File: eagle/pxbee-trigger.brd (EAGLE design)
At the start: 51 x 57 mm, 24 parts, among them J1 39501-1002, J2 39501-1009, K1 APAN3103, K2 APAN3103, K3 APAN3103, K4 APAN3103, Q1 BC548BTA, Q2 BC548BTA, Q3 BC548BTA, Q4 BC548BTA

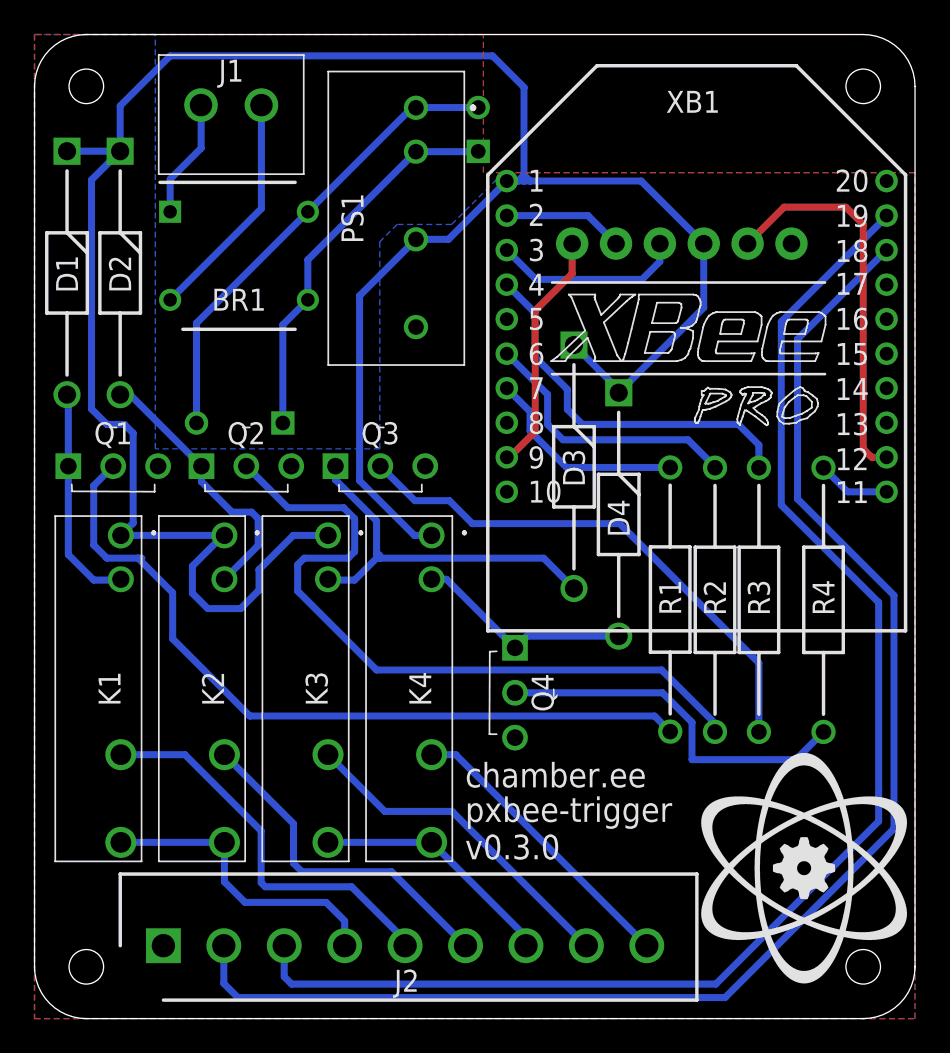
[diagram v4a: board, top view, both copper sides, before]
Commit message: Bridge rectifier upgrade; XBee reset header
- [Parts] Bridge rectifier upgraded from DF005 to DF01, previous part was underdimensioned
- [SCH,BRD] Added J3 pinout for XBee Reset
- [BRD] Version bumped to v0.4.0
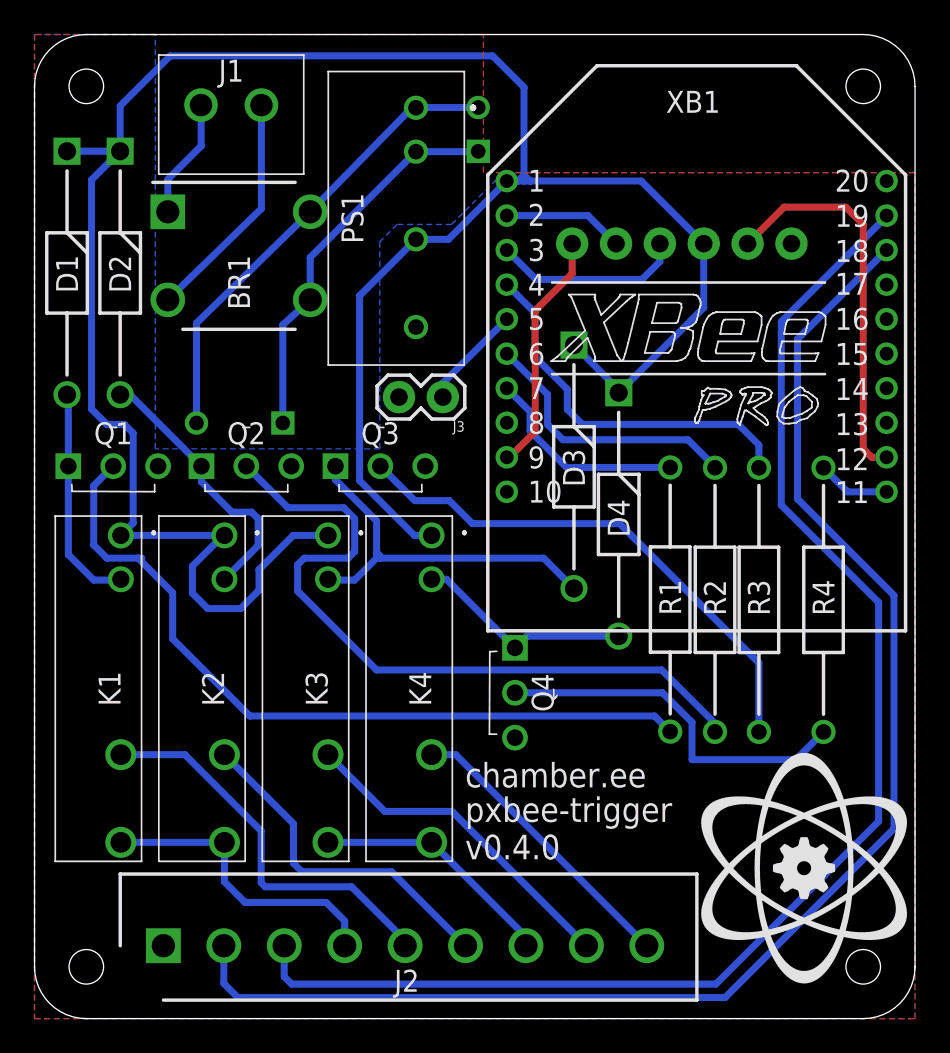
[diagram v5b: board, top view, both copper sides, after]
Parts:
- added J3: (no value), SparkFun-Connectors:1X02
- BR1: value DF005M -> DF01M; device parts:DIP798W58P510L828H330Q4N -> parts:DIP825W114P510L828H330Q4N
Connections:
- net DIO1 renamed STAT1
- net DIO2 renamed STAT2
- new net RST: J3.1, XB1.5
- net GND: now also J3.2
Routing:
- net RST: track 0.00 -> 6.05 mm
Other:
- board text added: "A1"
- board text added: "A2"
- board text added: "A3"
- board text added: "A4"
- board text added: "C1"
- board text added: "C2"
- board text added: "GND"
- board text added: "S1"
- board text added: "S2"
- board text added: "v0.4.0"
- board text removed: "v0.3.0"
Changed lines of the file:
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@@
 <text x="24.941" y="13.393" size="1.4224" layer="21" rot="R180" align="top-right">chamber.ee</text>
 <text x="24.941" y="11.393" size="1.4224" layer="21" rot="R180" align="top-right">pxbee-trigger</text>
-<text x="24.941" y="9.22755625" size="1.4224" layer="21" rot="R180" align="top-right">v0.3.0</text>
+<text x="24.941" y="9.22755625" size="1.4224" layer="21" rot="R180" align="top-right">v0.4.0</text>
 <hole x="3" y="3" drill="2"/>
 <hole x="48" y="3" drill="2"/>
@@
 <wire x1="3" y1="57" x2="0" y2="54" width="0" layer="20" curve="90"/>
 <wire x1="51" y1="54" x2="48" y2="57" width="0" layer="20" curve="90"/>
+<text x="8.746" y="1.873" size="0.8128" layer="22" rot="MR0">GND</text>
+<text x="11.746" y="1.873" size="0.8128" layer="22" rot="MR0">S2</text>
+<text x="15.113" y="1.905" size="0.8128" layer="22" rot="MR0">S1</text>
+<text x="18.655" y="1.81" size="0.8128" layer="22" rot="MR0">C1</text>
+<text x="22.388" y="1.842" size="0.8128" layer="22" rot="MR0">A1</text>
+<text x="25.661" y="1.874" size="0.8128" layer="22" rot="MR0">A2</text>
+<text x="32.661" y="1.874" size="0.8128" layer="22" rot="MR0">A3</text>
+<text x="36.237" y="1.906" size="0.8128" layer="22" rot="MR0">A4</text>
+<text x="29.246" y="1.842" size="0.8128" layer="22" rot="MR0">C2</text>
 </plain>
 <attributes>
@@
 </autorouter>
 <elements>
-<element name="BR1" library="parts" package="DIP798W58P510L828H330Q4N" value="DF005M" x="11.844" y="44.182" smashed="yes">
-<attribute name="DESCRIPTION" value="ON SEMICONDUCTOR - DF005M - BRIDGE RECTIFIER, 1.5A, 50V, 4DIP" x="75.344" y="39.102" size="1.778" layer="27" display="off"/>
+<element name="BR1" library="parts" package="DIP825W114P510L828H330Q4N" value="DF01M" x="11.844" y="44.182" smashed="yes">
+<attribute name="ARROW_PART_NUMBER" value="DF01M" x="11.844" y="44.182" size="1.778" layer="27" display="off"/>
+<attribute name="ARROW_PRICE-STOCK" value="https://www.arrow.com/en/products/df01m/on-semiconductor" x="11.844" y="44.182" size="1.778" layer="27" display="off"/>
+<attribute name="DESCRIPTION" value="ON SEMICONDUCTOR - DF01M - BRIDGE RECTIFIER, 1.5A, 100V, 4-DIP" x="75.344" y="39.102" size="1.778" layer="27" display="off"/>
 <attribute name="HEIGHT" value="3.3mm" x="75.344" y="39.102" size="1.778" layer="27" display="off"/>
 <attribute name="MANUFACTURER_NAME" value="ON Semiconductor" x="75.344" y="39.102" size="1.778" layer="27" display="off"/>
-<attribute name="MANUFACTURER_PART_NUMBER" value="DF005M" x="75.344" y="39.102" size="1.778" layer="27" display="off"/>
-<attribute name="MOUSER_PART_NUMBER" value="512-DF005M" x="75.344" y="39.102" size="1.778" layer="27" display="off"/>
-<attribute name="MOUSER_PRICE-STOCK" value="https://www.mouser.com/Search/Refine.aspx?Keyword=512-DF005M" x="75.344" y="39.102" size="1.778" layer="27" display="off"/>
-<attribute name="NAME" x="11.844" y="41.642" size="1.27" layer="25" align="center"/>
-<attribute name="RS_PART_NUMBER" value="9033686" x="75.344" y="39.102" size="1.778" layer="27" display="off"/>
-<attribute name="RS_PRICE-STOCK" value="http://uk.rs-online.com/web/p/products/9033686" x="75.344" y="39.102" size="1.778" layer="27" display="off"/>
+<attribute name="MANUFACTURER_PART_NUMBER" value="DF01M" x="75.344" y="39.102" size="1.778" layer="27" display="off"/>
+<attribute name="MOUSER_PART_NUMBER" value="512-DF01M" x="75.344" y="39.102" size="1.778" layer="27" display="off"/>
+<attribute name="MOUSER_PRICE-STOCK" value="https://www.mouser.co.uk/ProductDetail/ON-Semiconductor-Fairchild/DF01M?qs=jEaxvrTvpac4Wk7%2Fu%252BjpDQ%3D%3D" x="75.344" y="39.102" size="1.778" layer="27" display="off"/>
+<attribute name="NAME" x="11.844" y="42.642" size="1.27" layer="25" rot="R90" align="center"/>
 <attribute name="VALUE" x="11.844" y="46.722" size="1.27" layer="27" align="center"/>
 </element>
@@
 <attribute name="NAME" x="29.7958" y="42.0602" size="1.27" layer="26" ratio="10" rot="MR180"/>
 <attribute name="VALUE" x="29.872" y="48.064" size="1.27" layer="28" rot="MR180"/>
+</element>
+<element name="J3" library="SparkFun-Connectors" library_urn="urn:adsk.eagle:library:513" package="1X02" package3d_urn="urn:adsk.eagle:package:38039/1" value="" x="23.651" y="36" smashed="yes" rot="R180">
+<attribute name="NAME" x="24.921" y="34.603" size="0.6096" layer="25" font="vector" ratio="20" rot="R180"/>
+<attribute name="VALUE" x="24.921" y="38.032" size="0.6096" layer="27" font="vector" ratio="20" rot="R180"/>
 </element>
 </elements>
@@
 </polygon>
 <contactref element="JP1" pad="P$6"/>
+<contactref element="J3" pad="2"/>
+<wire x1="27.354" y1="30.513" x2="43.842" y2="44.889" width="0" layer="19" extent="1-1"/>
+<wire x1="22.631" y1="32" x2="27.354" y2="30.513" width="0" layer="19" extent="1-1"/>
+<wire x1="21.111" y1="36" x2="22.631" y2="32" width="0" layer="19" extent="1-1"/>
+<wire x1="22.095" y1="40.056" x2="21.111" y2="36" width="0" layer="19" extent="1-1"/>
+<wire x1="14.868" y1="32" x2="21.111" y2="36" width="0" layer="19" extent="1-1"/>
+<wire x1="7.158" y1="32" x2="14.868" y2="32" width="0" layer="19" extent="1-1"/>
+<wire x1="27.83" y1="16.273" x2="27.354" y2="30.513" width="0" layer="19" extent="1-1"/>
+<wire x1="7.465" y1="4.222" x2="27.83" y2="16.273" width="0" layer="19" extent="1-1"/>
 </signal>
 <signal name="N$1">
@@
 <contactref element="PS1" pad="1"/>
 <contactref element="C1" pad="2"/>
-<wire x1="15.832" y1="46.732" x2="21.856" y2="52.756" width="0.4064" layer="16"/>
+<wire x1="15.969" y1="46.732" x2="21.856" y2="52.756" width="0.4064" layer="16"/>
 <wire x1="21.856" y1="52.756" x2="22.095" y2="52.756" width="0.4064" layer="16"/>
 <wire x1="9.383" y1="34.499" x2="9.383" y2="40.283" width="0.4064" layer="16"/>
-<wire x1="9.383" y1="40.283" x2="15.832" y2="46.732" width="0.4064" layer="16"/>
+<wire x1="9.383" y1="40.283" x2="15.969" y2="46.732" width="0.4064" layer="16"/>
 <contactref element="C2" pad="2"/>
 <wire x1="25.7" y1="52.772" x2="22.111" y2="52.772" width="0.4064" layer="16"/>
@@
 <contactref element="PS1" pad="2"/>
 <contactref element="C1" pad="1"/>
-<wire x1="22.095" y1="50.216" x2="15.832" y2="43.953" width="0.4064" layer="16"/>
-<wire x1="15.832" y1="43.953" x2="15.832" y2="41.632" width="0.4064" layer="16"/>
+<wire x1="22.095" y1="50.216" x2="15.966078125" y2="44.087078125" width="0.4064" layer="16"/>
+<wire x1="15.969" y1="44.037584375" x2="15.966078125" y2="44.087078125" width="0.4064" layer="16"/>
+<wire x1="15.969" y1="44.037584375" x2="15.969" y2="41.632" width="0.4064" layer="16"/>
 <wire x1="14.383" y1="34.499" x2="14.383" y2="40.183" width="0.4064" layer="16"/>
-<wire x1="14.383" y1="40.183" x2="15.832" y2="41.632" width="0.4064" layer="16"/>
+<wire x1="14.383" y1="40.183" x2="15.969" y2="41.632" width="0.4064" layer="16"/>
 <contactref element="C2" pad="1"/>
 <wire x1="25.7" y1="50.232" x2="25.684" y2="50.216" width="0.4064" layer="16"/>
@@
 <contactref element="BR1" pad="1"/>
 <contactref element="J1" pad="2"/>
-<wire x1="7.856" y1="46.732" x2="7.856" y2="48.623" width="0.4064" layer="16"/>
-<wire x1="7.856" y1="48.623" x2="9.652" y2="50.419" width="0.4064" layer="16"/>
-<wire x1="9.652" y1="50.419" x2="9.652" y2="52.903" width="0.4064" layer="16"/>
+<wire x1="7.719" y1="46.732" x2="7.719" y2="48.484971875" width="0.4064" layer="16"/>
+<wire x1="7.729" y1="48.623" x2="7.719" y2="48.484971875" width="0.4064" layer="16"/>
+<wire x1="7.729" y1="48.623" x2="9.652" y2="50.546" width="0.4064" layer="16"/>
+<wire x1="9.652" y1="50.546" x2="9.652" y2="52.903" width="0.4064" layer="16"/>
 <wire x1="9.652" y1="52.903" x2="9.643" y2="52.912" width="0.4064" layer="16"/>
 </signal>
@@
 <contactref element="BR1" pad="2"/>
 <contactref element="J1" pad="1"/>
-<wire x1="7.856" y1="41.632" x2="13.143" y2="46.919" width="0.4064" layer="16"/>
+<wire x1="7.719" y1="41.632" x2="13.143" y2="46.919" width="0.4064" layer="16"/>
 <wire x1="13.143" y1="46.919" x2="13.143" y2="52.912" width="0.4064" layer="16"/>
 </signal>
-<signal name="DIO2">
+<signal name="STAT2">
 <contactref element="XB1" pad="18"/>
 <contactref element="J2" pad="2"/>
@@
 <wire x1="11.7808" y1="1.2192" x2="10.965" y2="2.035" width="0.4064" layer="16"/>
 </signal>
-<signal name="DIO1">
+<signal name="STAT1">
 <contactref element="XB1" pad="19"/>
 <contactref element="J2" pad="3"/>
@@
 <wire x1="29.053" y1="42.814" x2="27.354" y2="44.513" width="0.4064" layer="16"/>
 </signal>
+<signal name="RST">
+<contactref element="XB1" pad="5"/>
+<contactref element="J3" pad="1"/>
+<wire x1="23.651" y1="36" x2="23.651" y2="36.81" width="0.4064" layer="16"/>
+<wire x1="23.651" y1="36.81" x2="27.354" y2="40.513" width="0.4064" layer="16"/>
+</signal>
 </signals>
